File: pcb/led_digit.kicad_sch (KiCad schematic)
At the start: 23 parts

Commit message: PCB layout work
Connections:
- net +5V is gone; now on net +5VE: D55.1 (VDD), D56.1 (VDD)
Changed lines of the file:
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@@
   (junction (at 115.57 170.18) (diameter 0) (color 0 0 0 0)
-  )
-  (junction (at 80.01 104.14) (diameter 0) (color 0 0 0 0)
   )
   (junction (at 102.87 165.1) (diameter 0) (color 0 0 0 0)
@@
     (effects (font (size 1.27 1.27)) (justify left))
     (property "Intersheet References" "${INTERSHEET_REFS}" (id 0) (at 75.0094 156.3974 90)
+      (effects (font (size 1.27 1.27)) (justify left) hide)
+    )
+  )
+  (global_label "+5VE" (shape input) (at 80.01 104.14 90) (fields_autoplaced)
+    (effects (font (size 1.27 1.27)) (justify left))
+    (property "Intersheet References" "${INTERSHEET_REFS}" (id 0) (at 80.0894 96.7074 90)
       (effects (font (size 1.27 1.27)) (justify left) hide)
     )
@@
     (pin "4")
   )
-  (symbol (lib_id "power:+5V") (at 80.01 104.14 0) (unit 1)
-    (in_bom yes) (on_board yes) (fields_autoplaced)
-    (property "Reference" "#PWR0141" (id 0) (at 80.01 107.95 0)
-      (effects (font (size 1.27 1.27)) hide)
-    )
-    (property "Value" "+5V" (id 1) (at 80.01 100.33 0))
-    (property "Footprint" "" (id 2) (at 80.01 104.14 0)
-      (effects (font (size 1.27 1.27)) hide)
-    )
-    (property "Datasheet" "" (id 3) (at 80.01 104.14 0)
-      (effects (font (size 1.27 1.27)) hide)
-    )
-    (pin "1")
-  )
   (symbol (lib_id "power:GND") (at 95.25 120.65 0) (mirror y) (unit 1)

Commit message: Finished layout
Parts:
- D53, D54, D55, D56, D57, D58, D59, D60, D61, D62, D63, D64, D65, D66, D67: footprint LED_SMD:LED_Kingbright_AAA3528ESGCT -> XL-3528RGBW-WS2812B:XL-3528RGBW-WS2812B
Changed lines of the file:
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@@
       (effects (font (size 1.27 1.27)) hide)
     )
-    (property "Footprint" "LED_SMD:LED_Kingbright_AAA3528ESGCT" (id 2) (at 157.48 156.21 0)
+    (property "Footprint" "XL-3528RGBW-WS2812B:XL-3528RGBW-WS2812B" (id 2) (at 157.48 156.21 0)
       (effects (font (size 1.27 1.27)) (justify left top) hide)
     )
@@
       (effects (font (size 1.27 1.27)) hide)
     )
-    (property "Footprint" "LED_SMD:LED_Kingbright_AAA3528ESGCT" (id 2) (at 121.92 99.06 0)
+    (property "Footprint" "XL-3528RGBW-WS2812B:XL-3528RGBW-WS2812B" (id 2) (at 121.92 99.06 0)
       (effects (font (size 1.27 1.27)) (justify left top) hide)
     )
@@
     (property "Reference" "D57" (id 0) (at 109.22 40.64 0))
     (property "Value" "WS2812B" (id 1) (at 110.49 53.34 0))
-    (property "Footprint" "LED_SMD:LED_Kingbright_AAA3528ESGCT" (id 2) (at 105.41 54.61 0)
+    (property "Footprint" "XL-3528RGBW-WS2812B:XL-3528RGBW-WS2812B" (id 2) (at 105.41 54.61 0)
       (effects (font (size 1.27 1.27)) (justify left top) hide)
     )
@@
       (effects (font (size 1.27 1.27)) hide)
     )
-    (property "Footprint" "LED_SMD:LED_Kingbright_AAA3528ESGCT" (id 2) (at 128.27 120.65 0)
+    (property "Footprint" "XL-3528RGBW-WS2812B:XL-3528RGBW-WS2812B" (id 2) (at 128.27 120.65 0)
       (effects (font (size 1.27 1.27)) (justify left top) hide)
     )
@@
       (effects (font (size 1.27 1.27)) hide)
     )
-    (property "Footprint" "LED_SMD:LED_Kingbright_AAA3528ESGCT" (id 2) (at 95.25 102.87 0)
+    (property "Footprint" "XL-3528RGBW-WS2812B:XL-3528RGBW-WS2812B" (id 2) (at 95.25 102.87 0)
       (effects (font (size 1.27 1.27)) (justify left top) hide)
     )
@@
       (effects (font (size 1.27 1.27)) hide)
     )
-    (property "Footprint" "LED_SMD:LED_Kingbright_AAA3528ESGCT" (id 2) (at 106.68 99.06 0)
+    (property "Footprint" "XL-3528RGBW-WS2812B:XL-3528RGBW-WS2812B" (id 2) (at 106.68 99.06 0)
       (effects (font (size 1.27 1.27)) (justify left top) hide)
     )
@@
       (effects (font (size 1.27 1.27)) hide)
     )
-    (property "Footprint" "LED_SMD:LED_Kingbright_AAA3528ESGCT" (id 2) (at 95.25 62.23 0)
+    (property "Footprint" "XL-3528RGBW-WS2812B:XL-3528RGBW-WS2812B" (id 2) (at 95.25 62.23 0)
       (effects (font (size 1.27 1.27)) (justify left top) hide)
     )
@@
       (effects (font (size 1.27 1.27)) hide)
     )
-    (property "Footprint" "LED_SMD:LED_Kingbright_AAA3528ESGCT" (id 2) (at 95.25 77.47 0)
+    (property "Footprint" "XL-3528RGBW-WS2812B:XL-3528RGBW-WS2812B" (id 2) (at 95.25 77.47 0)
       (effects (font (size 1.27 1.27)) (justify left top) hide)
     )
@@
       (effects (font (size 1.27 1.27)) hide)
     )
-    (property "Footprint" "LED_SMD:LED_Kingbright_AAA3528ESGCT" (id 2) (at 128.27 105.41 0)
+    (property "Footprint" "XL-3528RGBW-WS2812B:XL-3528RGBW-WS2812B" (id 2) (at 128.27 105.41 0)
       (effects (font (size 1.27 1.27)) (justify left top) hide)
     )
@@
       (effects (font (size 1.27 1.27)) hide)
     )
-    (property "Footprint" "LED_SMD:LED_Kingbright_AAA3528ESGCT" (id 2) (at 120.65 54.61 0)
+    (property "Footprint" "XL-3528RGBW-WS2812B:XL-3528RGBW-WS2812B" (id 2) (at 120.65 54.61 0)
       (effects (font (size 1.27 1.27)) (justify left top) hide)
     )
@@
       (effects (font (size 1.27 1.27)) hide)
     )
-    (property "Footprint" "LED_SMD:LED_Kingbright_AAA3528ESGCT" (id 2) (at 95.25 118.11 0)
+    (property "Footprint" "XL-3528RGBW-WS2812B:XL-3528RGBW-WS2812B" (id 2) (at 95.25 118.11 0)
       (effects (font (size 1.27 1.27)) (justify left top) hide)
     )
@@
       (effects (font (size 1.27 1.27)) hide)
     )
-    (property "Footprint" "LED_SMD:LED_Kingbright_AAA3528ESGCT" (id 2) (at 128.27 64.77 0)
+    (property "Footprint" "XL-3528RGBW-WS2812B:XL-3528RGBW-WS2812B" (id 2) (at 128.27 64.77 0)
       (effects (font (size 1.27 1.27)) (justify left top) hide)
     )
@@
       (effects (font (size 1.27 1.27)) hide)
     )
-    (property "Footprint" "LED_SMD:LED_Kingbright_AAA3528ESGCT" (id 2) (at 128.27 80.01 0)
+    (property "Footprint" "XL-3528RGBW-WS2812B:XL-3528RGBW-WS2812B" (id 2) (at 128.27 80.01 0)
       (effects (font (size 1.27 1.27)) (justify left top) hide)
     )
@@
       (effects (font (size 1.27 1.27)) hide)
     )
-    (property "Footprint" "LED_SMD:LED_Kingbright_AAA3528ESGCT" (id 2) (at 118.11 146.05 0)
+    (property "Footprint" "XL-3528RGBW-WS2812B:XL-3528RGBW-WS2812B" (id 2) (at 118.11 146.05 0)
       (effects (font (size 1.27 1.27)) (justify left top) hide)
     )
@@
       (effects (font (size 1.27 1.27)) hide)
     )
-    (property "Footprint" "LED_SMD:LED_Kingbright_AAA3528ESGCT" (id 2) (at 102.87 146.05 0)
-      (effects (font (size 1.27 1.27)) (justify left top) hide)
-    )
+    (property "Footprint" "XL-3528RGBW-WS2812B:XL-3528RGBW-WS2812B" (id 2) (at 102.87 146.05 0)
+      (effects (font (size 1.27 1.27)) (justify left top) hide)
+    )

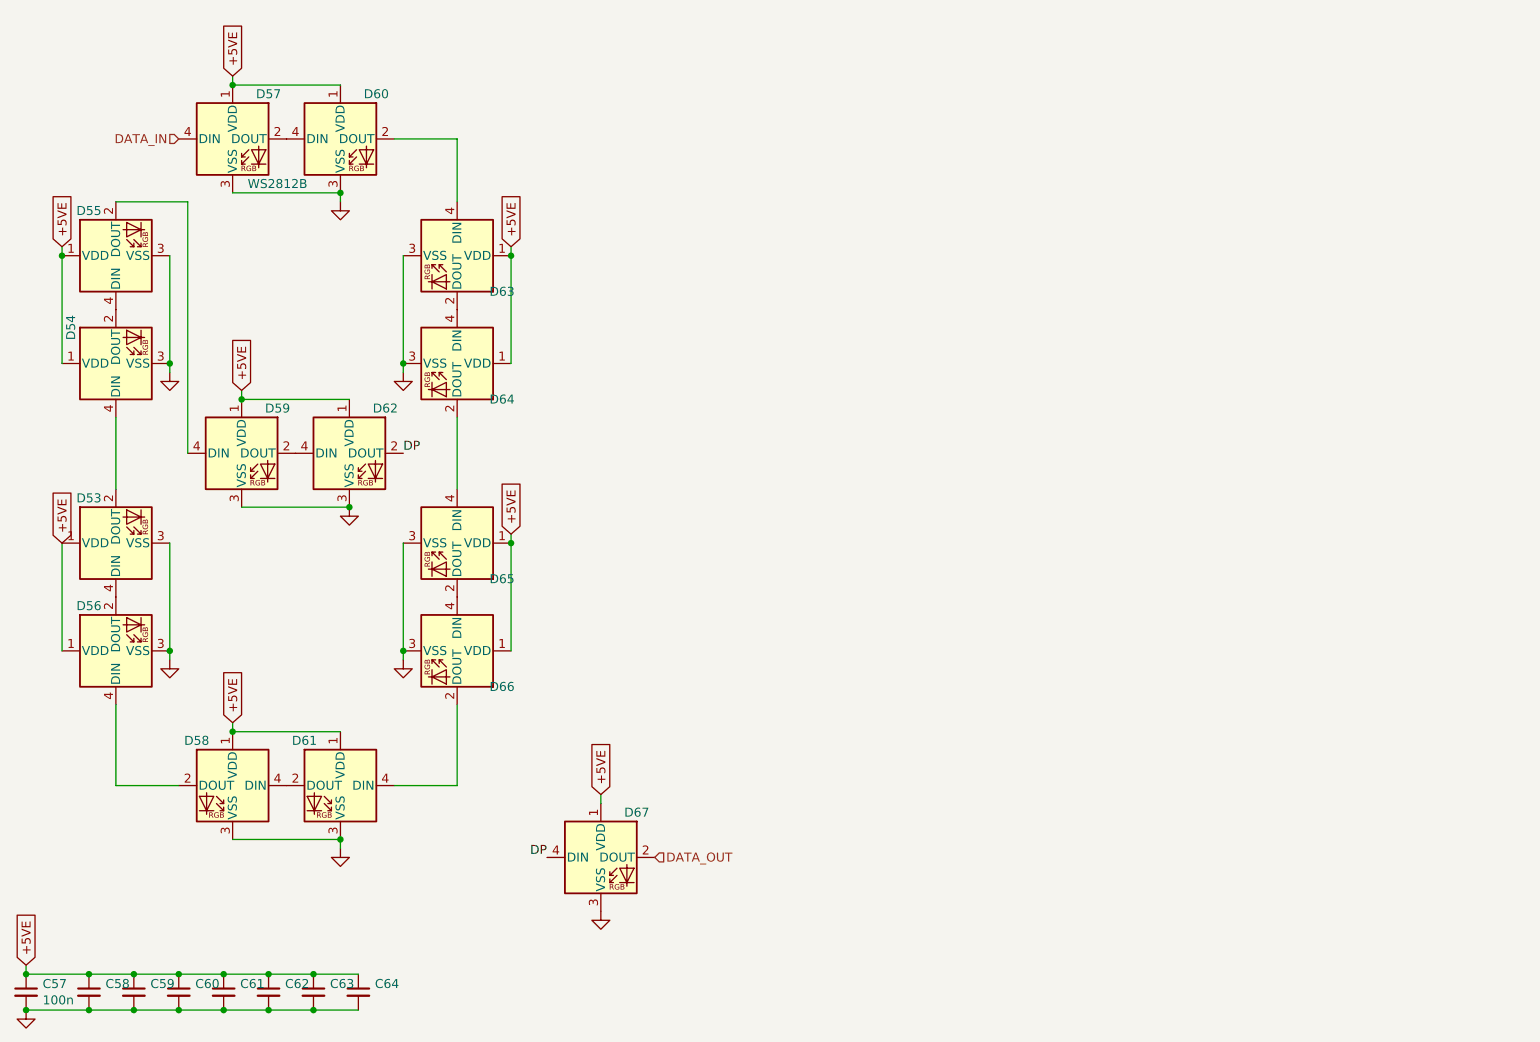
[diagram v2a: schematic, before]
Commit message: change to kicad 7, fix led signal direction for segment displays
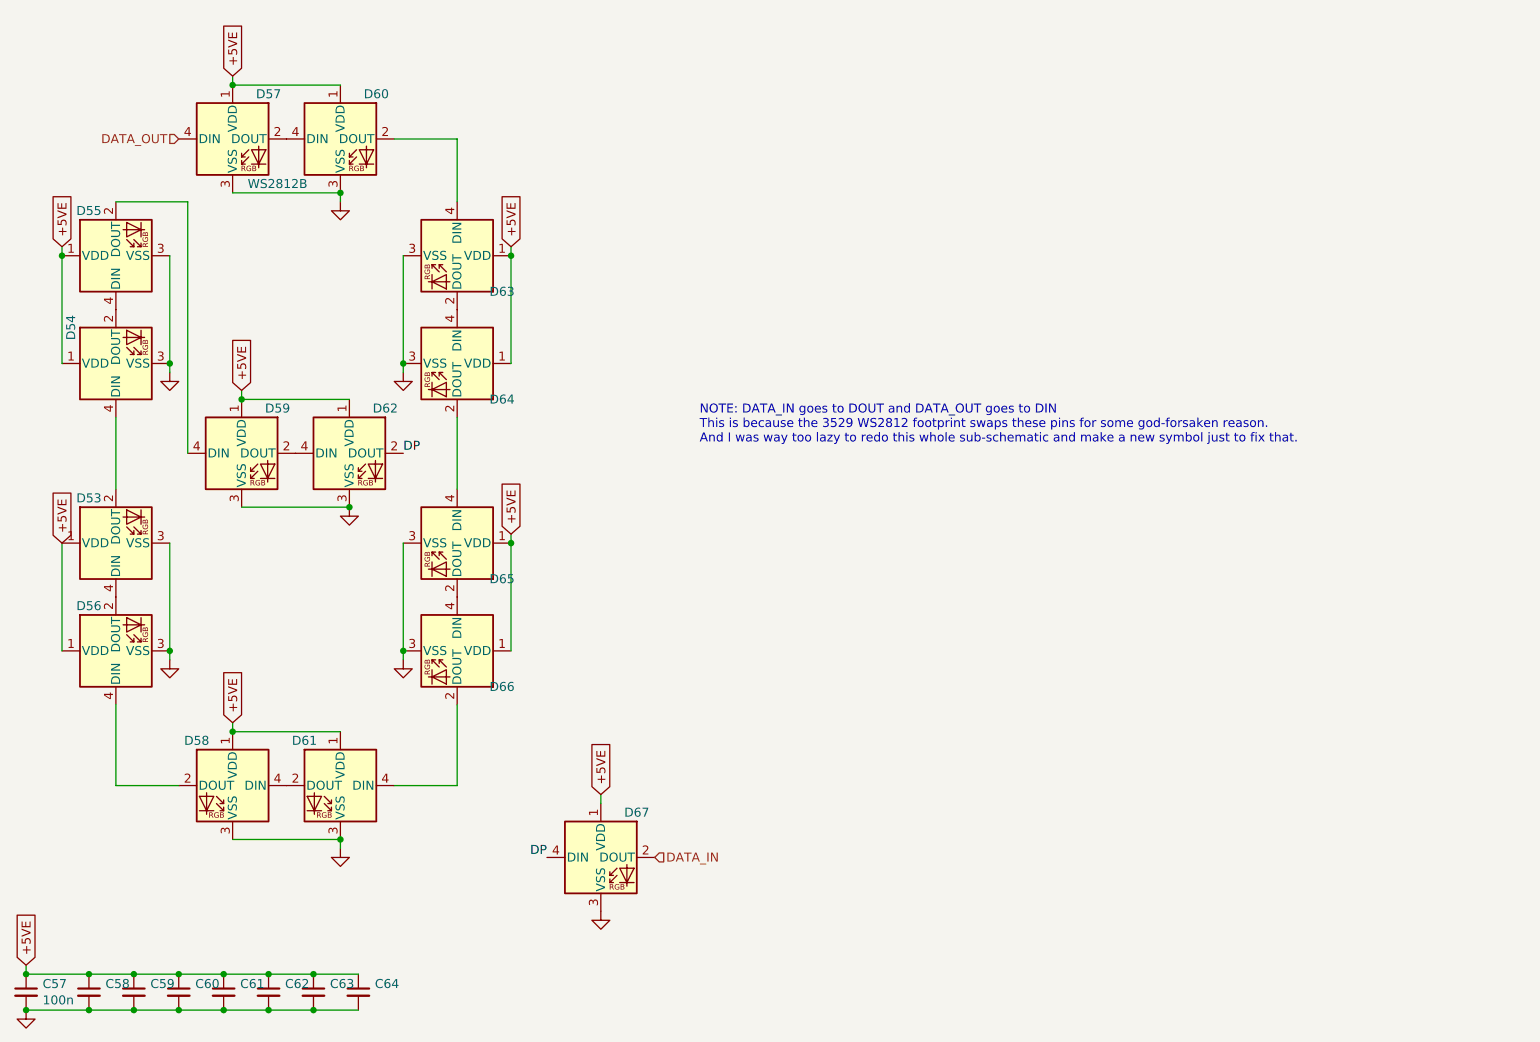
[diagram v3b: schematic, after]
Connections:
- net DATA_IN: now also D67.2 (DOUT); no longer D57.4 (DIN)
- net DATA_OUT: now also D57.4 (DIN); no longer D67.2 (DOUT)
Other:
- note added: "NOTE: DATA_IN goes to DOUT and DATA_OUT goes to DIN This is because the 3529 WS2812 footprint swaps these pins for some god-forsaken reason. And I was way too lazy to redo this whole sub-schematic and make a new symbol just to fix that."

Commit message: Fix kikad 7 schematic issues
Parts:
- D53, D54, D55, D56, D57, D58, D59, D60, D61, D62, D63, D64, D65, D66, D67: footprint XL-3528RGBW-WS2812B:XL-3528RGBW-WS2812B -> LED_SMD:LED_WS2812B_PLCC4_5.0x5.0mm_P3.2mm
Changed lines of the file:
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@@
       (effects (font (size 1.27 1.27)) hide)
     )
-    (property "Footprint" "XL-3528RGBW-WS2812B:XL-3528RGBW-WS2812B" (at 157.48 156.21 0)
+    (property "Footprint" "LED_SMD:LED_WS2812B_PLCC4_5.0x5.0mm_P3.2mm" (at 157.48 156.21 0)
       (effects (font (size 1.27 1.27)) (justify left top) hide)
     )
@@
       (effects (font (size 1.27 1.27)) hide)
     )
-    (property "Footprint" "XL-3528RGBW-WS2812B:XL-3528RGBW-WS2812B" (at 121.92 99.06 0)
+    (property "Footprint" "LED_SMD:LED_WS2812B_PLCC4_5.0x5.0mm_P3.2mm" (at 121.92 99.06 0)
       (effects (font (size 1.27 1.27)) (justify left top) hide)
     )
@@
       (effects (font (size 1.27 1.27)))
     )
-    (property "Footprint" "XL-3528RGBW-WS2812B:XL-3528RGBW-WS2812B" (at 105.41 54.61 0)
+    (property "Footprint" "LED_SMD:LED_WS2812B_PLCC4_5.0x5.0mm_P3.2mm" (at 105.41 54.61 0)
       (effects (font (size 1.27 1.27)) (justify left top) hide)
     )
@@
       (effects (font (size 1.27 1.27)) hide)
     )
-    (property "Footprint" "XL-3528RGBW-WS2812B:XL-3528RGBW-WS2812B" (at 128.27 120.65 0)
+    (property "Footprint" "LED_SMD:LED_WS2812B_PLCC4_5.0x5.0mm_P3.2mm" (at 128.27 120.65 0)
       (effects (font (size 1.27 1.27)) (justify left top) hide)
     )
@@
       (effects (font (size 1.27 1.27)) hide)
     )
-    (property "Footprint" "XL-3528RGBW-WS2812B:XL-3528RGBW-WS2812B" (at 95.25 102.87 0)
+    (property "Footprint" "LED_SMD:LED_WS2812B_PLCC4_5.0x5.0mm_P3.2mm" (at 95.25 102.87 0)
       (effects (font (size 1.27 1.27)) (justify left top) hide)
     )
@@
       (effects (font (size 1.27 1.27)) hide)
     )
-    (property "Footprint" "XL-3528RGBW-WS2812B:XL-3528RGBW-WS2812B" (at 106.68 99.06 0)
+    (property "Footprint" "LED_SMD:LED_WS2812B_PLCC4_5.0x5.0mm_P3.2mm" (at 106.68 99.06 0)
       (effects (font (size 1.27 1.27)) (justify left top) hide)
     )
@@
       (effects (font (size 1.27 1.27)) hide)
     )
-    (property "Footprint" "XL-3528RGBW-WS2812B:XL-3528RGBW-WS2812B" (at 95.25 62.23 0)
+    (property "Footprint" "LED_SMD:LED_WS2812B_PLCC4_5.0x5.0mm_P3.2mm" (at 95.25 62.23 0)
       (effects (font (size 1.27 1.27)) (justify left top) hide)
     )
@@
       (effects (font (size 1.27 1.27)) hide)
     )
-    (property "Footprint" "XL-3528RGBW-WS2812B:XL-3528RGBW-WS2812B" (at 95.25 77.47 0)
+    (property "Footprint" "LED_SMD:LED_WS2812B_PLCC4_5.0x5.0mm_P3.2mm" (at 95.25 77.47 0)
       (effects (font (size 1.27 1.27)) (justify left top) hide)
     )
@@
       (effects (font (size 1.27 1.27)) hide)
     )
-    (property "Footprint" "XL-3528RGBW-WS2812B:XL-3528RGBW-WS2812B" (at 128.27 105.41 0)
+    (property "Footprint" "LED_SMD:LED_WS2812B_PLCC4_5.0x5.0mm_P3.2mm" (at 128.27 105.41 0)
       (effects (font (size 1.27 1.27)) (justify left top) hide)
     )
@@
       (effects (font (size 1.27 1.27)) hide)
     )
-    (property "Footprint" "XL-3528RGBW-WS2812B:XL-3528RGBW-WS2812B" (at 120.65 54.61 0)
+    (property "Footprint" "LED_SMD:LED_WS2812B_PLCC4_5.0x5.0mm_P3.2mm" (at 120.65 54.61 0)
       (effects (font (size 1.27 1.27)) (justify left top) hide)
     )
@@
       (effects (font (size 1.27 1.27)) hide)
     )
-    (property "Footprint" "XL-3528RGBW-WS2812B:XL-3528RGBW-WS2812B" (at 95.25 118.11 0)
+    (property "Footprint" "LED_SMD:LED_WS2812B_PLCC4_5.0x5.0mm_P3.2mm" (at 95.25 118.11 0)
       (effects (font (size 1.27 1.27)) (justify left top) hide)
     )
@@
       (effects (font (size 1.27 1.27)) hide)
     )
-    (property "Footprint" "XL-3528RGBW-WS2812B:XL-3528RGBW-WS2812B" (at 128.27 64.77 0)
+    (property "Footprint" "LED_SMD:LED_WS2812B_PLCC4_5.0x5.0mm_P3.2mm" (at 128.27 64.77 0)
       (effects (font (size 1.27 1.27)) (justify left top) hide)
     )
@@
       (effects (font (size 1.27 1.27)) hide)
     )
-    (property "Footprint" "XL-3528RGBW-WS2812B:XL-3528RGBW-WS2812B" (at 128.27 80.01 0)
+    (property "Footprint" "LED_SMD:LED_WS2812B_PLCC4_5.0x5.0mm_P3.2mm" (at 128.27 80.01 0)
       (effects (font (size 1.27 1.27)) (justify left top) hide)
     )
@@
       (effects (font (size 1.27 1.27)) hide)
     )
-    (property "Footprint" "XL-3528RGBW-WS2812B:XL-3528RGBW-WS2812B" (at 118.11 146.05 0)
+    (property "Footprint" "LED_SMD:LED_WS2812B_PLCC4_5.0x5.0mm_P3.2mm" (at 118.11 146.05 0)
       (effects (font (size 1.27 1.27)) (justify left top) hide)
     )
@@
       (effects (font (size 1.27 1.27)) hide)
     )
-    (property "Footprint" "XL-3528RGBW-WS2812B:XL-3528RGBW-WS2812B" (at 102.87 146.05 0)
-      (effects (font (size 1.27 1.27)) (justify left top) hide)
-    )
+    (property "Footprint" "LED_SMD:LED_WS2812B_PLCC4_5.0x5.0mm_P3.2mm" (at 102.87 146.05 0)
+      (effects (font (size 1.27 1.27)) (justify left top) hide)
+    )
